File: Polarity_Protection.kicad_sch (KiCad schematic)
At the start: 7 parts, among them J1 IN+, J2 IN-, Q1 BSS214NW

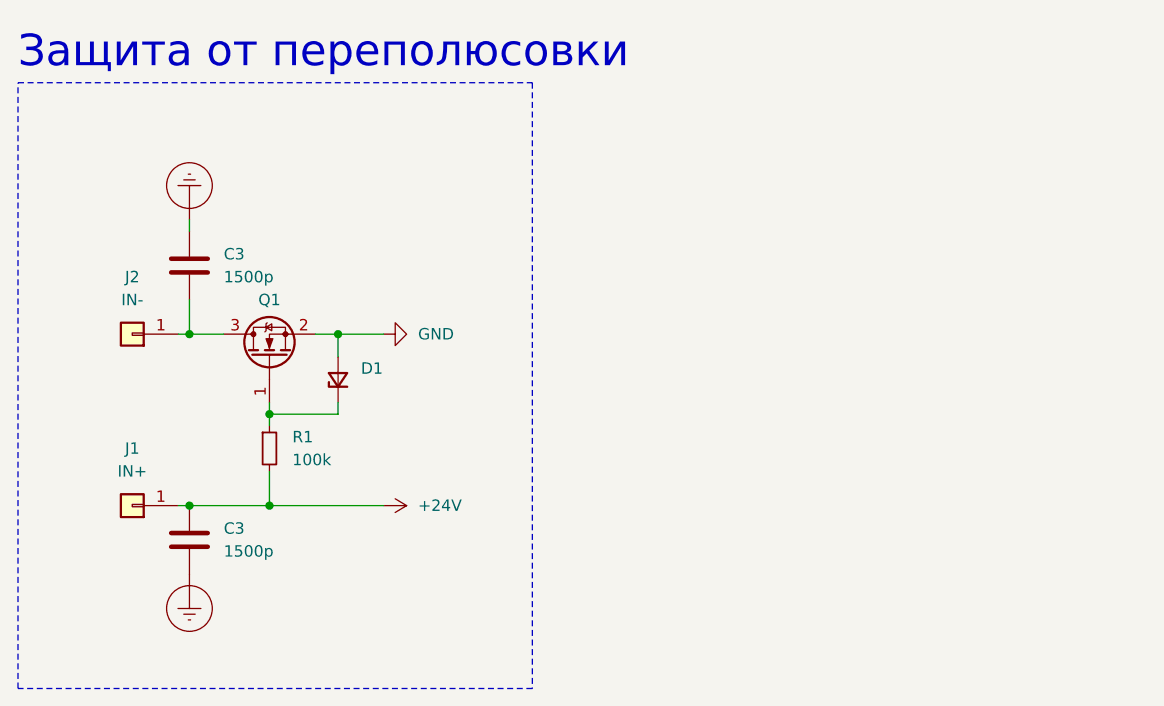
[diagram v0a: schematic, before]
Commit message: Заменил разъёмы 2.54 на 1.27мм
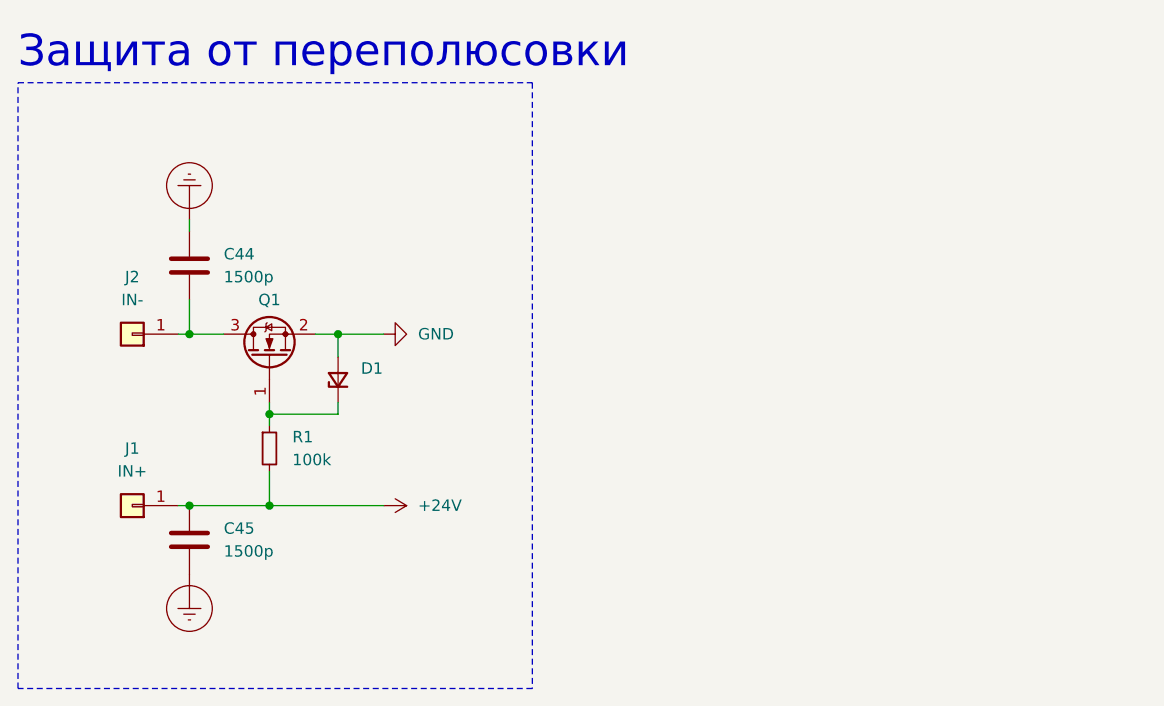
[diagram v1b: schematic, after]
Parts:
- renumbered C3 to C44, C3 to C45

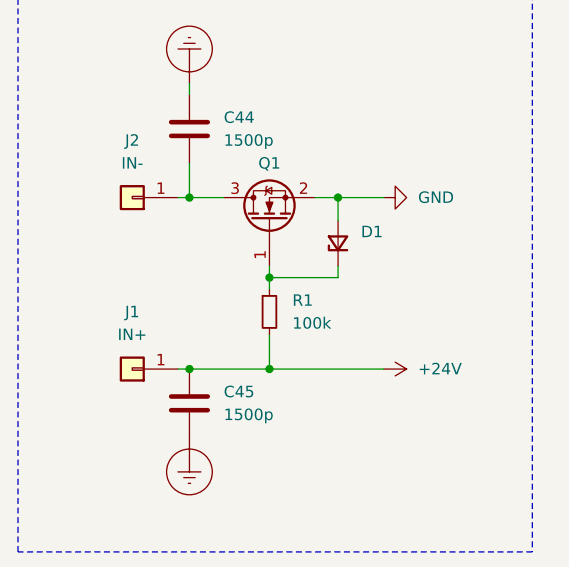
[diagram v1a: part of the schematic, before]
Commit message: Добавил мегаомные резисторы
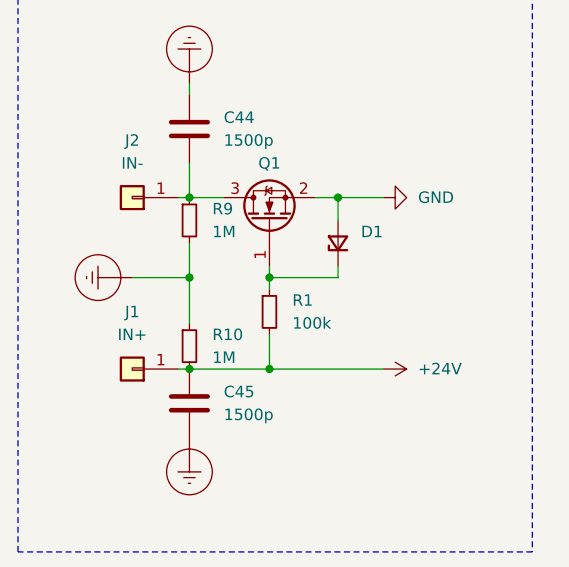
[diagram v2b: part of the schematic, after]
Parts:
- added R10, R9: 1M, Resistor_SMD:R_0805_2012Metric_Pad1.20x1.40mm_HandSolder, symbol Device:R_Small
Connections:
- net +24V: now also R10.2
- net Earth_Protective: now also R10.1, R9.2
- net at C44.2, J2.1 (Pin_1), Q1.3 (D): now also R9.1
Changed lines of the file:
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@@
+	)
+	(junction
+		(at 143.51 104.14)
+		(diameter 0)
+		(color 0 0 0 0)
 	)
 	(junction
@@
 	(wire
 		(pts
+			(xy 143.51 104.14) (xy 143.51 100.33)
+		)
+		(stroke
+			(width 0)
+			(type default)
+		)
+	)
+	(wire
+		(pts
 			(xy 143.51 95.25) (xy 147.32 95.25)
 		)
@@
 	(wire
 		(pts
+			(xy 143.51 104.14) (xy 143.51 109.22)
+		)
+		(stroke
+			(width 0)
+			(type default)
+		)
+	)
+	(wire
+		(pts
 			(xy 160.02 95.25) (xy 165.1 95.25)
 		)
@@
 		(pts
 			(xy 143.51 114.3) (xy 152.4 114.3)
+		)
+		(stroke
+			(width 0)
+			(type default)
+		)
+	)
+	(wire
+		(pts
+			(xy 137.16 104.14) (xy 143.51 104.14)
 		)
 		(stroke
@@
 	)
 	(symbol
+		(lib_id "Device:R_Small")
+		(at 143.51 111.76 0)
+		(unit 1)
+		(exclude_from_sim no)
+		(in_bom yes)
+		(on_board yes)
+		(dnp no)
+		(fields_autoplaced yes)
+		(property "Reference" "R10"
+			(at 146.05 110.49 0)
+			(effects
+				(font
+					(size 1.27 1.27)
+				)
+				(justify left)
+			)
+		)
+		(property "Value" "1M"
+			(at 146.05 113.03 0)
+			(effects
+				(font
+					(size 1.27 1.27)
+				)
+				(justify left)
+			)
+		)
+		(property "Footprint" "Resistor_SMD:R_0805_2012Metric_Pad1.20x1.40mm_HandSolder"
+			(at 143.51 111.76 0)
+			(effects
+				(font
+					(size 1.27 1.27)
+				)
+				(hide yes)
+			)
+		)
+		(property "Datasheet" "~"
+			(at 143.51 111.76 0)
+			(effects
+				(font
+					(size 1.27 1.27)
+				)
+				(hide yes)
+			)
+		)
+		(property "Description" ""
+			(at 143.51 111.76 0)
+			(effects
+				(font
+					(size 1.27 1.27)
+				)
+				(hide yes)
+			)
+		)
+		(pin "1"
+		)
+		(pin "2"
+		)
+		(instances
+			(project "Силовая плата"
+				(path "/96c6fc92-8ec6-44f7-b0dc-9ad8f1acea09/1efb5faf-bb82-4ac6-a144-d6576b4720aa"
+					(reference "R10")
+					(unit 1)
+				)
+			)
+		)
+	)
+	(symbol
 		(lib_id "power:Earth_Protective")
 		(at 143.51 121.92 0)
@@
 	)
 	(symbol
+		(lib_id "Device:R_Small")
+		(at 143.51 97.79 0)
+		(unit 1)
+		(exclude_from_sim no)
+		(in_bom yes)
+		(on_board yes)
+		(dnp no)
+		(fields_autoplaced yes)
+		(property "Reference" "R9"
+			(at 146.05 96.52 0)
+			(effects
+				(font
+					(size 1.27 1.27)
+				)
+				(justify left)
+			)
+		)
+		(property "Value" "1M"
+			(at 146.05 99.06 0)
+			(effects
+				(font
+					(size 1.27 1.27)
+				)
+				(justify left)
+			)
+		)
+		(property "Footprint" "Resistor_SMD:R_0805_2012Metric_Pad1.20x1.40mm_HandSolder"
+			(at 143.51 97.79 0)
+			(effects
+				(font
+					(size 1.27 1.27)
+				)
+				(hide yes)
+			)
+		)
+		(property "Datasheet" "~"
+			(at 143.51 97.79 0)
+			(effects
+				(font
+					(size 1.27 1.27)
+				)
+				(hide yes)
+			)
+		)
+		(property "Description" ""
+			(at 143.51 97.79 0)
+			(effects
+				(font
+					(size 1.27 1.27)
+				)
+				(hide yes)
+			)
+		)
+		(pin "1"
+		)
+		(pin "2"
+		)
+		(instances
+			(project "Силовая плата"
+				(path "/96c6fc92-8ec6-44f7-b0dc-9ad8f1acea09/1efb5faf-bb82-4ac6-a144-d6576b4720aa"
+					(reference "R9")
+					(unit 1)
+				)
+			)
+		)
+	)
+	(symbol
 		(lib_id "power:Earth_Protective")
 		(at 143.51 82.55 180)
@@
 					(unit 1)
 				)
+			)
+		)
+	)
+	(symbol
+		(lib_id "power:Earth_Protective")
+		(at 137.16 104.14 270)
+		(unit 1)
+		(exclude_from_sim no)
+		(in_bom yes)
+		(on_board yes)
+		(dnp no)
+		(fields_autoplaced yes)
+		(property "Reference" "#PWR030"
+			(at 130.81 110.49 0)
+			(effects
+				(font
+					(size 1.27 1.27)
+				)
+				(hide yes)
+			)
+		)
+		(property "Value" "Earth_Protective"
+			(at 133.35 115.57 0)
+			(effects
+				(font
+					(size 1.27 1.27)
+				)
+				(hide yes)
+			)
+		)
+		(property "Footprint" ""
+			(at 134.62 104.14 0)
+			(effects
+				(font
+					(size 1.27 1.27)
+				)
+				(hide yes)
+			)
+		)
+		(property "Datasheet" "~"
+			(at 134.62 104.14 0)
+			(effects
+				(font
+					(size 1.27 1.27)
+				)
+				(hide yes)
+			)
+		)
+		(property "Description" ""
+			(at 137.16 104.14 0)
+			(effects
+				(font
+					(size 1.27 1.27)
+				)
+				(hide yes)
+			)
+		)
+		(pin "1"
+		)
+		(instances
+			(project "Силовая плата"
+				(path "/96c6fc92-8ec6-44f7-b0dc-9ad8f1acea09/1efb5faf-bb82-4ac6-a144-d6576b4720aa"
+					(reference "#PWR030")
+					(unit 1)
+				)
